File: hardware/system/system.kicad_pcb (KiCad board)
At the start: 2 copper layers, 226.6 x 87.2 mm, 51 parts, among them J1 CART_SOCKET_28P, J2 EXT_PINS, SW1 POWER, SW2 RESET, SW3 A, SW4 B, SW5 UP, SW6 DN, SW7 LF, SW8 RT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

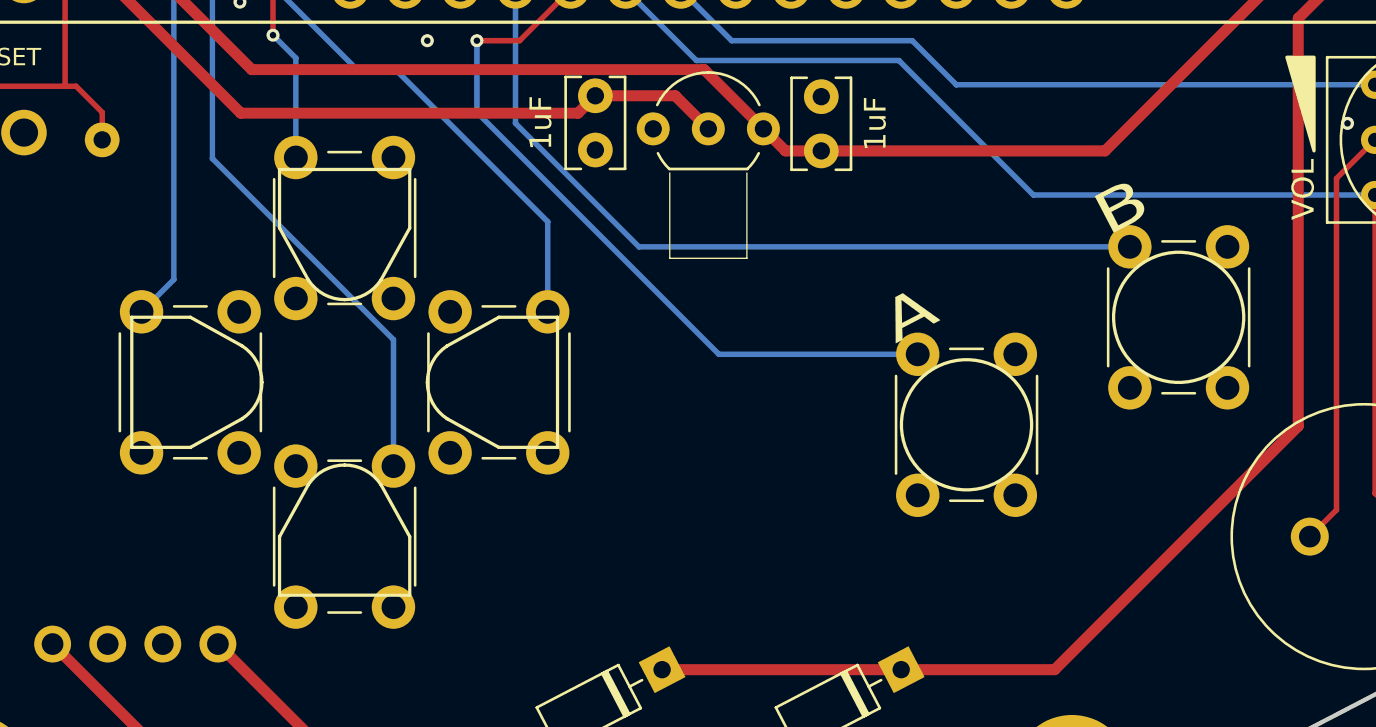
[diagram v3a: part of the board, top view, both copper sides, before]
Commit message: Update main board button labels
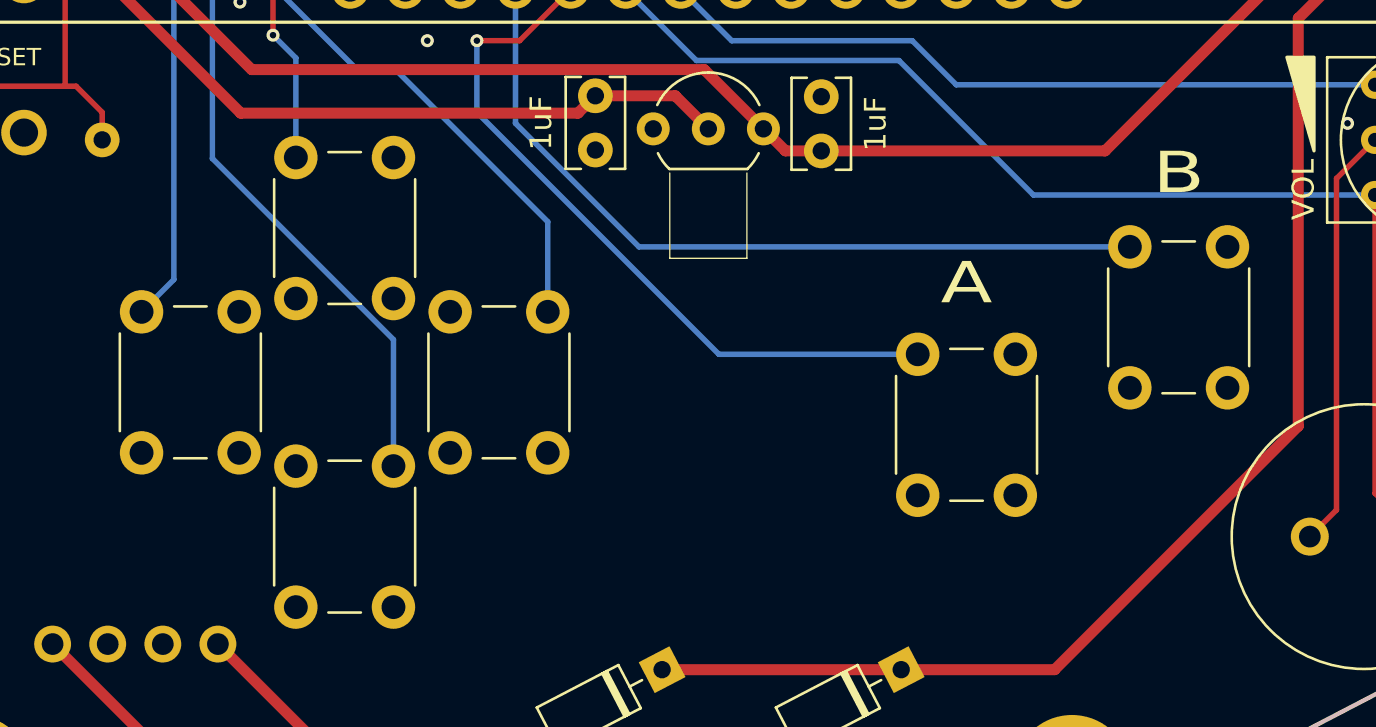
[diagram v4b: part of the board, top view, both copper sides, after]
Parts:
- removed the REF** at (130.0, 133.1)
- removed the REF** at (122.9, 140.2)
- removed the REF** at (115.8, 133.1)
- removed the REF** at (122.9, 126.0)
- removed the REF** at (161.4, 130.1)
- removed the REF** at (151.6, 135.1)
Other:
- board text added: "A"
- board text added: "B"
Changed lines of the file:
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@@
   (general
     (thickness 1.6)
-    (drawings 107)
+    (drawings 109)
     (tracks 172)
     (zones 0)
-    (modules 51)
+    (modules 45)
     (nets 28)
   )
   (page USLetter)
   (layers
-    (0 F.Cu signal)
+    (0 F.Cu signal hide)
     (31 B.Cu signal hide)
     (32 B.Adhes user)
@@
     )
   )
-  (module system:OMRON_CAP_B32-2110 (layer F.Cu)
-    (at 130.048 133.096 180)
-    (fp_text reference REF** (at 0 6.985) (layer F.Fab) hide
-      (effects (font (size 1 1) (thickness 0.15)))
-    )
-    (fp_text value OMRON_CAP_B32-2110 (at 0 -6.985) (layer F.Fab) hide
-      (effects (font (size 1 1) (thickness 0.15)))
-    )
-    (fp_line (start -2.7 -3) (end -2.7 3) (layer F.SilkS) (width 0.15))
-    (fp_line (start -2.7 -3) (end 0 -3) (layer F.SilkS) (width 0.15))
-    (fp_line (start -2.7 3) (end 0 3) (layer F.SilkS) (width 0.15))
-    (fp_line (start 0 -3) (end 2.391059 -1.676183) (layer F.SilkS) (width 0.15))
-    (fp_line (start 0 3) (end 2.392204 1.675437) (layer F.SilkS) (width 0.15))
-    (fp_line (start -2.95 -2.5) (end -2.95 2.5) (layer F.Fab) (width 0.1))
-    (fp_line (start -2.2 -3.25) (end -0.320046 -3.251318) (layer F.Fab) (width 0.1))
-    (fp_line (start 0.35052 -3.09626) (end 2.528729 -1.884867) (layer F.Fab) (width 0.1))
-    (fp_line (start -2.2 3.25) (end -0.320046 3.248682) (layer F.Fab) (width 0.1))
-    (fp_line (start 0.349882 3.093604) (end 2.528729 1.884867) (layer F.Fab) (width 0.1))
-    (fp_arc (start -0.255493 2.002985) (end -0.320046 3.248682) (angle -32) (layer F.Fab) (width 0.1))
-    (fp_arc (start -0.255493 -2.002985) (end 0.35052 -3.09626) (angle -31.9602417) (layer F.Fab) (width 0.1))
-    (fp_arc (start -2.2 2.5) (end -2.2 3.25) (angle 90) (layer F.Fab) (width 0.1))
-    (fp_arc (start -2.2 -2.5) (end -2.95 -2.5) (angle 90) (layer F.Fab) (width 0.1))
-    (fp_arc (start 1.3 0) (end 3.55 0) (angle 56.9) (layer F.Fab) (width 0.1))
-    (fp_arc (start 1.3 0) (end 3.55 0) (angle -56.9) (layer F.Fab) (width 0.1))
-    (fp_arc (start 1.3 0) (end 3.3 0) (angle 56.9) (layer F.SilkS) (width 0.15))
-    (fp_arc (start 1.3 0) (end 3.3 0) (angle -56.93914698) (layer F.SilkS) (width 0.15))
-  )
-  (module system:OMRON_CAP_B32-2110 (layer F.Cu)
-    (at 122.936 140.208 90)
-    (fp_text reference REF** (at 0 6.985 90) (layer F.Fab) hide
-      (effects (font (size 1 1) (thickness 0.15)))
-    )
-    (fp_text value OMRON_CAP_B32-2110 (at 0 -6.985 90) (layer F.Fab) hide
-      (effects (font (size 1 1) (thickness 0.15)))
-    )
-    (fp_line (start 0.349882 3.093604) (end 2.528729 1.884867) (layer F.Fab) (width 0.1))
-    (fp_line (start -2.2 3.25) (end -0.320046 3.248682) (layer F.Fab) (width 0.1))
-    (fp_line (start 0.35052 -3.09626) (end 2.528729 -1.884867) (layer F.Fab) (width 0.1))
-    (fp_line (start -2.2 -3.25) (end -0.320046 -3.251318) (layer F.Fab) (width 0.1))
-    (fp_line (start -2.95 -2.5) (end -2.95 2.5) (layer F.Fab) (width 0.1))
-    (fp_line (start 0 3) (end 2.392204 1.675437) (layer F.SilkS) (width 0.15))
-    (fp_line (start 0 -3) (end 2.391059 -1.676183) (layer F.SilkS) (width 0.15))
-    (fp_line (start -2.7 3) (end 0 3) (layer F.SilkS) (width 0.15))
-    (fp_line (start -2.7 -3) (end 0 -3) (layer F.SilkS) (width 0.15))
-    (fp_line (start -2.7 -3) (end -2.7 3) (layer F.SilkS) (width 0.15))
-    (fp_arc (start 1.3 0) (end 3.3 0) (angle -56.93914698) (layer F.SilkS) (width 0.15))
-    (fp_arc (start 1.3 0) (end 3.3 0) (angle 56.9) (layer F.SilkS) (width 0.15))
-    (fp_arc (start 1.3 0) (end 3.55 0) (angle -56.9) (layer F.Fab) (width 0.1))
-    (fp_arc (start 1.3 0) (end 3.55 0) (angle 56.9) (layer F.Fab) (width 0.1))
-    (fp_arc (start -2.2 -2.5) (end -2.95 -2.5) (angle 90) (layer F.Fab) (width 0.1))
-    (fp_arc (start -2.2 2.5) (end -2.2 3.25) (angle 90) (layer F.Fab) (width 0.1))
-    (fp_arc (start -0.255493 -2.002985) (end 0.35052 -3.09626) (angle -31.9602417) (layer F.Fab) (width 0.1))
-    (fp_arc (start -0.255493 2.002985) (end -0.320046 3.248682) (angle -32) (layer F.Fab) (width 0.1))
-  )
-  (module system:OMRON_CAP_B32-2110 (layer F.Cu)
-    (at 115.824 133.096)
-    (fp_text reference REF** (at 0 6.985) (layer F.Fab) hide
-      (effects (font (size 1 1) (thickness 0.15)))
-    )
-    (fp_text value OMRON_CAP_B32-2110 (at 0 -6.985) (layer F.Fab) hide
-      (effects (font (size 1 1) (thickness 0.15)))
-    )
-    (fp_line (start 0.349882 3.093604) (end 2.528729 1.884867) (layer F.Fab) (width 0.1))
-    (fp_line (start -2.2 3.25) (end -0.320046 3.248682) (layer F.Fab) (width 0.1))
-    (fp_line (start 0.35052 -3.09626) (end 2.528729 -1.884867) (layer F.Fab) (width 0.1))
-    (fp_line (start -2.2 -3.25) (end -0.320046 -3.251318) (layer F.Fab) (width 0.1))
-    (fp_line (start -2.95 -2.5) (end -2.95 2.5) (layer F.Fab) (width 0.1))
-    (fp_line (start 0 3) (end 2.392204 1.675437) (layer F.SilkS) (width 0.15))
-    (fp_line (start 0 -3) (end 2.391059 -1.676183) (layer F.SilkS) (width 0.15))
-    (fp_line (start -2.7 3) (end 0 3) (layer F.SilkS) (width 0.15))
-    (fp_line (start -2.7 -3) (end 0 -3) (layer F.SilkS) (width 0.15))
-    (fp_line (start -2.7 -3) (end -2.7 3) (layer F.SilkS) (width 0.15))
-    (fp_arc (start 1.3 0) (end 3.3 0) (angle -56.93914698) (layer F.SilkS) (width 0.15))
-    (fp_arc (start 1.3 0) (end 3.3 0) (angle 56.9) (layer F.SilkS) (width 0.15))
-    (fp_arc (start 1.3 0) (end 3.55 0) (angle -56.9) (layer F.Fab) (width 0.1))
-    (fp_arc (start 1.3 0) (end 3.55 0) (angle 56.9) (layer F.Fab) (width 0.1))
-    (fp_arc (start -2.2 -2.5) (end -2.95 -2.5) (angle 90) (layer F.Fab) (width 0.1))
-    (fp_arc (start -2.2 2.5) (end -2.2 3.25) (angle 90) (layer F.Fab) (width 0.1))
-    (fp_arc (start -0.255493 -2.002985) (end 0.35052 -3.09626) (angle -31.9602417) (layer F.Fab) (width 0.1))
-    (fp_arc (start -0.255493 2.002985) (end -0.320046 3.248682) (angle -32) (layer F.Fab) (width 0.1))
-  )
-  (module system:OMRON_CAP_B32-2110 (layer F.Cu)
-    (at 122.936 125.984 270)
-    (fp_text reference REF** (at 0 6.985 90) (layer F.Fab) hide
-      (effects (font (size 1 1) (thickness 0.15)))
-    )
-    (fp_text value OMRON_CAP_B32-2110 (at 0 -6.985 90) (layer F.Fab) hide
-      (effects (font (size 1 1) (thickness 0.15)))
-    )
-    (fp_line (start -2.7 -3) (end -2.7 3) (layer F.SilkS) (width 0.15))
-    (fp_line (start -2.7 -3) (end 0 -3) (layer F.SilkS) (width 0.15))
-    (fp_line (start -2.7 3) (end 0 3) (layer F.SilkS) (width 0.15))
-    (fp_line (start 0 -3) (end 2.391059 -1.676183) (layer F.SilkS) (width 0.15))
-    (fp_line (start 0 3) (end 2.392204 1.675437) (layer F.SilkS) (width 0.15))
-    (fp_line (start -2.95 -2.5) (end -2.95 2.5) (layer F.Fab) (width 0.1))
-    (fp_line (start -2.2 -3.25) (end -0.320046 -3.251318) (layer F.Fab) (width 0.1))
-    (fp_line (start 0.35052 -3.09626) (end 2.528729 -1.884867) (layer F.Fab) (width 0.1))
-    (fp_line (start -2.2 3.25) (end -0.320046 3.248682) (layer F.Fab) (width 0.1))
-    (fp_line (start 0.349882 3.093604) (end 2.528729 1.884867) (layer F.Fab) (width 0.1))
-    (fp_arc (start -0.255493 2.002985) (end -0.320046 3.248682) (angle -32) (layer F.Fab) (width 0.1))
-    (fp_arc (start -0.255493 -2.002985) (end 0.35052 -3.09626) (angle -31.9602417) (layer F.Fab) (width 0.1))
-    (fp_arc (start -2.2 2.5) (end -2.2 3.25) (angle 90) (layer F.Fab) (width 0.1))
-    (fp_arc (start -2.2 -2.5) (end -2.95 -2.5) (angle 90) (layer F.Fab) (width 0.1))
-    (fp_arc (start 1.3 0) (end 3.55 0) (angle 56.9) (layer F.Fab) (width 0.1))
-    (fp_arc (start 1.3 0) (end 3.55 0) (angle -56.9) (layer F.Fab) (width 0.1))
-    (fp_arc (start 1.3 0) (end 3.3 0) (angle 56.9) (layer F.SilkS) (width 0.15))
-    (fp_arc (start 1.3 0) (end 3.3 0) (angle -56.93914698) (layer F.SilkS) (width 0.15))
-  )
-  (module system:OMRON_CAP_B32-2010 (layer F.Cu)
-    (at 161.381 130.1 27.5)
-    (fp_text reference REF** (at 0 5.08 27.5) (layer F.Fab) hide
-      (effects (font (size 1 1) (thickness 0.15)))
-    )
-    (fp_text value OMRON_CAP_B32-2010 (at 0 -5.08 27.5) (layer F.Fab) hide
-      (effects (font (size 1 1) (thickness 0.15)))
-    )
-    (fp_circle (center 0 0) (end 3 0) (layer F.SilkS) (width 0.15))
-    (fp_circle (center 0 0) (end 3.25 0) (layer F.Fab) (width 0.1))
-    (fp_text user B (at 0 -5.715 27.5) (layer F.SilkS)
-      (effects (font (size 1.905 2.54) (thickness 0.381)))
-    )
-  )
-  (module system:OMRON_CAP_B32-2010 (layer F.Cu)
-    (at 151.602 135.053 27.5)
-    (fp_text reference REF** (at 0 5.08 27.5) (layer F.Fab) hide
-      (effects (font (size 1 1) (thickness 0.15)))
-    )
-    (fp_text value OMRON_CAP_B32-2010 (at 0 -5.08 27.5) (layer F.Fab) hide
-      (effects (font (size 1 1) (thickness 0.15)))
-    )
-    (fp_circle (center 0 0) (end 3 0) (layer F.SilkS) (width 0.15))
-    (fp_circle (center 0 0) (end 3.25 0) (layer F.Fab) (width 0.1))
-    (fp_text user A (at 0 -5.715 27.5) (layer F.SilkS)
-      (effects (font (size 1.905 2.54) (thickness 0.381)))
-    )
-  )
   (module MountingHole:MountingHole_2.7mm_M2.5_Pad (layer F.Cu)
     (at 105.791 151.13)
@@
     )
   )
+  (gr_text B (at 161.381 123.444) (layer F.SilkS)
+    (effects (font (size 1.905 2.54) (thickness 0.381)))
+  )
+  (gr_text A (at 151.602 128.524) (layer F.SilkS)
+    (effects (font (size 1.905 2.54) (thickness 0.381)))
+  )
   (gr_text "Arduboy CE" (at 216.0905 127.254) (layer B.SilkS)

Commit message: Add JLC order number lables
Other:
- board text added: "JLCJLCJLCJLC"
